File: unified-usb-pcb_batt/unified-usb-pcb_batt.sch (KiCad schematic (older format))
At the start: 38 parts, among them J1 QI, J2 USB_C_Receptacle_USB2.0, J3 USB_Out, J4 BATT, J5 THERM, SW1 SW_SPDT, U1 SRV05-4, U2 DW01A, U3 TP4056, U4 FS8205

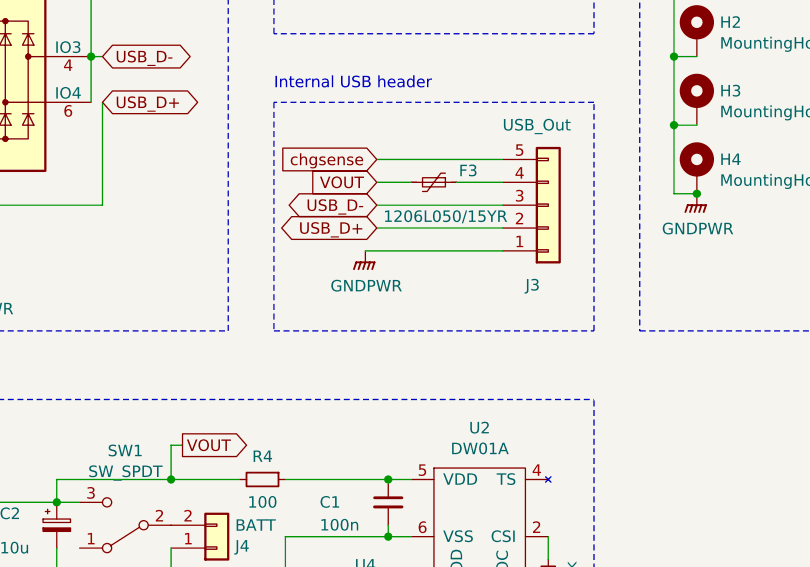
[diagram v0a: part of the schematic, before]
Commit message: added ferrite bead
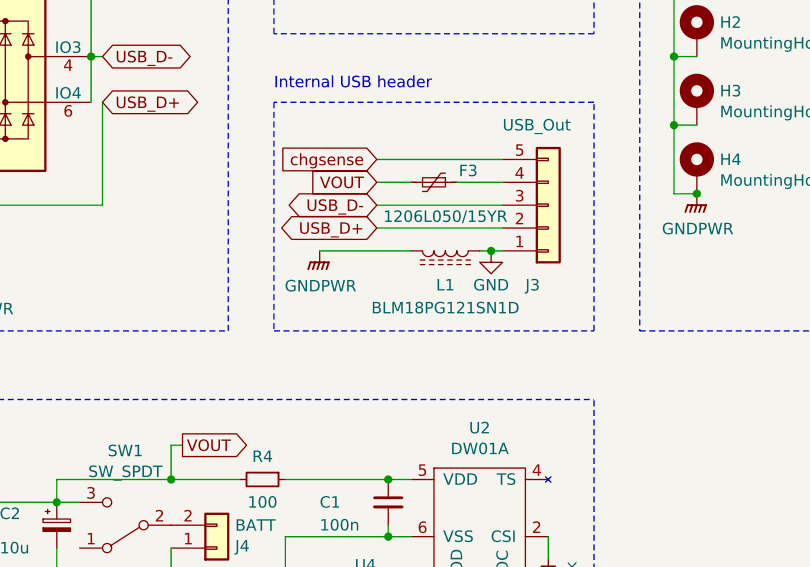
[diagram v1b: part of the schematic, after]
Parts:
- added L1: BLM18PG121SN1D, Inductor_SMD:L_0603_1608Metric, symbol Device:L_Core_Ferrite
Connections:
- net GNDPWR: now also L1.2; no longer J3.1 (Pin_1)
- new net GND: J3.1 (Pin_1), L1.1
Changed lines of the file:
@@
 L power:GNDPWR #PWR05
 U 1 1 5E879D91
-P 4550 2500
-F 0 "#PWR05" H 4550 2300 50  0001 C CNN
-F 1 "GNDPWR" H 4554 2346 50  0000 C CNN
-F 2 "" H 4550 2450 50  0001 C CNN
-F 3 "" H 4550 2450 50  0001 C CNN
-	1    4550 2500
-	1    0    0    -1
-$EndComp
-Wire Wire Line
-	5150 2500 4550 2500
+P 4350 2500
+F 0 "#PWR05" H 4350 2300 50  0001 C CNN
+F 1 "GNDPWR" H 4354 2346 50  0000 C CNN
+F 2 "" H 4350 2450 50  0001 C CNN
+F 3 "" H 4350 2450 50  0001 C CNN
+	1    4350 2500
+	1    0    0    -1
+$EndComp
 Text GLabel 4600 2100 0    50   Input ~ 0
 chgsense
@@
 Text Notes 5750 650  0    50   ~ 0
 Mounting Holes
+$Comp
+L Device:L_Core_Ferrite L1
+U 1 1 5E8FEF9F
+P 4900 2500
+F 0 "L1" V 5050 2500 50  0000 C CNN
+F 1 "BLM18PG121SN1D" V 5150 2500 50  0000 C CNN
+F 2 "Inductor_SMD:L_0603_1608Metric" H 4900 2500 50  0001 C CNN
+F 3 "~" H 4900 2500 50  0001 C CNN
+	1    4900 2500
+	0    1    1    0
+$EndComp
+Wire Wire Line
+	5150 2500 5100 2500
+Wire Wire Line
+	4750 2500 4350 2500
+$Comp
+L power:GND #PWR0102
+U 1 1 5E908A81
+P 5100 2500
+F 0 "#PWR0102" H 5100 2250 50  0001 C CNN
+F 1 "GND" H 5100 2350 50  0000 C CNN
+F 2 "" H 5100 2500 50  0001 C CNN
+F 3 "" H 5100 2500 50  0001 C CNN
+	1    5100 2500
+	1    0    0    -1
+$EndComp
+Connection ~ 5100 2500
+Wire Wire Line
+	5100 2500 5050 2500
 $EndSCHEMATC

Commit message: added jlcpcb part numbers
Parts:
- C1, C4: LCSC (none) -> C14663
- C2, C3: LCSC (none) -> C7171
- D1, D2: LCSC (none) -> C8678
- D3: LCSC (none) -> C72043
- D4: LCSC (none) -> C2286
- F1, F2, F3: LCSC (none) -> C151162
- H1, H2, H3, H4, J1, J2, J3, J4, J5, JP1, JP2, SW1: LCSC (none) -> /
- L1: LCSC (none) -> C73100
- R1, R2: LCSC (none) -> C23186
- R10: LCSC (none) -> C4177
- R11: LCSC (none) -> C31850
- R3: LCSC (none) -> C21189
- R4: LCSC (none) -> C22775
- R5, R7: LCSC (none) -> C13167
- R6: LCSC (none) -> C25804
- R8: LCSC (none) -> C22978
- R9: LCSC (none) -> C21190
- U1: LCSC (none) -> C85364
- U2: LCSC (none) -> C14213
- U3: LCSC (none) -> C16581
- U4: LCSC (none) -> C32254
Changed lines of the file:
@@
 F 2 "Connector_USB:USB_C_Receptacle_HRO_TYPE-C-31-M-12" H 1250 1700 50  0001 C CNN
 F 3 "https://www.usb.org/sites/default/files/documents/usb_type-c.zip" H 1250 1700 50  0001 C CNN
+F 4 "/" H 1100 1700 50  0001 C CNN "LCSC"
 	1    1100 1700
 	1    0    0    -1
@@
 F 2 "Package_TO_SOT_SMD:SOT-23-6" H 3550 1300 50  0001 C CNN
 F 3 "http://www.onsemi.com/pub/Collateral/SRV05-4-D.PDF" H 2850 1750 50  0001 C CNN
+F 4 "C85364" H 2850 1750 50  0001 C CNN "LCSC"
 	1    2850 1750
 	1    0    0    -1
@@
 F 2 "Resistor_SMD:R_0603_1608Metric" H 950 2600 50  0001 C CNN
 F 3 "~" H 950 2600 50  0001 C CNN
+F 4 "C21189" H 950 2600 50  0001 C CNN "LCSC"
 	1    950  2600
 	0    1    1    0
@@
 F 2 "Resistor_SMD:R_0603_1608Metric" H 1850 1300 50  0001 C CNN
 F 3 "~" H 1850 1300 50  0001 C CNN
+F 4 "C23186" H 1850 1300 50  0001 C CNN "LCSC"
 	1    1850 1300
 	0    1    1    0
@@
 F 2 "Resistor_SMD:R_0603_1608Metric" H 1850 1400 50  0001 C CNN
 F 3 "~" H 1850 1400 50  0001 C CNN
+F 4 "C23186" H 1850 1400 50  0001 C CNN "LCSC"
 	1    1850 1400
 	0    1    1    0
@@
 F 2 "Diode_SMD:D_SMA" H 3000 1100 50  0001 C CNN
 F 3 "https://datasheet.lcsc.com/szlcsc/Vishay-Intertech-SS36-E3-57T_C35722.pdf" H 3000 1100 50  0001 C CNN
+F 4 "C8678" H 3000 1100 50  0001 C CNN "LCSC"
 	1    3000 1100
 	-1   0    0    1
@@
 F 2 "Connector_JST:JST_SH_SM05B-SRSS-TB_1x05-1MP_P1.00mm_Horizontal" H 5350 2300 50  0001 C CNN
 F 3 "~" H 5350 2300 50  0001 C CNN
+F 4 "/" H 5350 2300 50  0001 C CNN "LCSC"
 	1    5350 2300
 	1    0    0    1
@@
 F 2 "Connector_JST:JST_SH_SM02B-SRSS-TB_1x02-1MP_P1.00mm_Horizontal" H 3900 3800 50  0001 C CNN
 F 3 "~" H 3900 3800 50  0001 C CNN
+F 4 "/" H 3900 3800 50  0001 C CNN "LCSC"
 	1    3900 3800
 	1    0    0    1
@@
 F 2 "Connector_JST:JST_SH_SM02B-SRSS-TB_1x02-1MP_P1.00mm_Horizontal" H 3400 4050 50  0001 C CNN
 F 3 "~" H 3400 4050 50  0001 C CNN
+F 4 "/" H 3400 4050 50  0001 C CNN "LCSC"
 	1    3400 4050
 	1    0    0    -1
@@
 F 2 "Connector_JST:JST_SH_SM02B-SRSS-TB_1x02-1MP_P1.00mm_Horizontal" H 4350 1200 50  0001 C CNN
 F 3 "~" H 4350 1200 50  0001 C CNN
+F 4 "/" H 4350 1200 50  0001 C CNN "LCSC"
 	1    4350 1200
 	-1   0    0    1
@@
 F 2 "Diode_SMD:D_SMA" H 5000 1100 50  0001 C CNN
 F 3 "https://datasheet.lcsc.com/szlcsc/Vishay-Intertech-SS36-E3-57T_C35722.pdf" H 5000 1100 50  0001 C CNN
+F 4 "C8678" H 5000 1100 50  0001 C CNN "LCSC"
 	1    5000 1100
 	-1   0    0    1
@@
 F 2 "Fuse:Fuse_1206_3216Metric" H 4750 900 50  0001 L CNN
 F 3 "https://datasheet.lcsc.com/szlcsc/1810252220_Fuzetec-Tech-FSMD050-1206-R_C220147.pdf" H 4700 1100 50  0001 C CNN
+F 4 "C151162" H 4700 1100 50  0001 C CNN "LCSC"
 	1    4700 1100
 	0    1    1    0
@@
 F 2 "Resistor_SMD:R_0603_1608Metric" H 650 3900 50  0001 C CNN
 F 3 "~" H 650 3900 50  0001 C CNN
+F 4 "C13167" H 650 3900 50  0001 C CNN "LCSC"
 	1    650  3900
 	-1   0    0    1
@@
 F 2 "Resistor_SMD:R_0603_1608Metric" H 1100 3900 50  0001 C CNN
 F 3 "~" H 1100 3900 50  0001 C CNN
+F 4 "C13167" H 1100 3900 50  0001 C CNN "LCSC"
 	1    1100 3900
 	-1   0    0    1
@@
 F 2 "LED_SMD:LED_0603_1608Metric_Castellated" V 650 3700 50  0001 C CNN
 F 3 "~" V 650 3700 50  0001 C CNN
+F 4 "C72043" H 650 3700 50  0001 C CNN "LCSC"
 	1    650  3700
 	0    -1   -1   0
@@
 F 2 "LED_SMD:LED_0603_1608Metric_Castellated" V 1100 3700 50  0001 C CNN
 F 3 "~" V 1100 3700 50  0001 C CNN
+F 4 "C2286" H 1100 3700 50  0001 C CNN "LCSC"
 	1    1100 3700
 	0    -1   -1   0
@@
 F 2 "Resistor_SMD:R_0603_1608Metric" H 2550 4250 50  0001 C CNN
 F 3 "~" H 2550 4250 50  0001 C CNN
+F 4 "C4177" H 2550 4250 50  0001 C CNN "LCSC"
 	1    2550 4250
 	-1   0    0    1
@@
 F 2 "Jumper:SolderJumper-2_P1.3mm_Open_RoundedPad1.0x1.5mm" H 3000 4250 50  0001 C CNN
 F 3 "~" H 3000 4250 50  0001 C CNN
+F 4 "/" H 3000 4250 50  0001 C CNN "LCSC"
 	1    3000 4250
 	0    1    1    0
@@
 F 2 "Jumper:SolderJumper-2_P1.3mm_Open_RoundedPad1.0x1.5mm" H 3050 900 50  0001 C CNN
 F 3 "~" H 3050 900 50  0001 C CNN
+F 4 "/" H 3050 900 50  0001 C CNN "LCSC"
 	1    3050 900
 	-1   0    0    1
@@
 F 2 "Resistor_SMD:R_0603_1608Metric" H 2800 3950 50  0001 C CNN
 F 3 "~" H 2800 3950 50  0001 C CNN
+F 4 "C22978" H 2800 3950 50  0001 C CNN "LCSC"
 	1    2800 3950
 	-1   0    0    1
@@
 F 2 "Resistor_SMD:R_0603_1608Metric" H 2800 4250 50  0001 C CNN
 F 3 "~" H 2800 4250 50  0001 C CNN
+F 4 "C31850" H 2800 4250 50  0001 C CNN "LCSC"
 	1    2800 4250
 	-1   0    0    1
@@
 F 2 "Capacitor_Tantalum_SMD:CP_EIA-3216-18_Kemet-A" H 1400 3800 50  0001 C CNN
 F 3 "~" H 1400 3800 50  0001 C CNN
+F 4 "C7171" H 1400 3800 50  0001 C CNN "LCSC"
 	1    1400 3800
 	1    0    0    -1
@@
 F 2 "Capacitor_SMD:C_0603_1608Metric" H 4650 3600 50  0001 C CNN
 F 3 "~" H 4650 3600 50  0001 C CNN
+F 4 "C14663" H 4650 3600 50  0001 C CNN "LCSC"
 	1    4650 3600
 	1    0    0    -1
@@
 F 2 "Resistor_SMD:R_0603_1608Metric" H 5350 3950 50  0001 C CNN
 F 3 "~" H 5350 3950 50  0001 C CNN
+F 4 "C21190" H 5350 3950 50  0001 C CNN "LCSC"
 	1    5350 3950
 	-1   0    0    1
@@
 F 2 "Resistor_SMD:R_0603_1608Metric" H 4100 3500 50  0001 C CNN
 F 3 "~" H 4100 3500 50  0001 C CNN
+F 4 "C22775" H 4100 3500 50  0001 C CNN "LCSC"
 	1    4100 3500
 	0    1    1    0
@@
 F 2 "Capacitor_Tantalum_SMD:CP_EIA-3216-18_Kemet-A" H 3200 3700 50  0001 C CNN
 F 3 "~" H 3200 3700 50  0001 C CNN
+F 4 "C7171" H 3200 3700 50  0001 C CNN "LCSC"
 	1    3200 3700
 	1    0    0    -1
@@
 F 2 "Capacitor_SMD:C_0603_1608Metric" H 1650 3800 50  0001 C CNN
 F 3 "~" H 1650 3800 50  0001 C CNN
+F 4 "C14663" H 1650 3800 50  0001 C CNN "LCSC"
 	1    1650 3800
 	1    0    0    -1
@@
 F 2 "Fuse:Fuse_1206_3216Metric" H 1900 900 50  0001 L CNN
 F 3 "https://datasheet.lcsc.com/szlcsc/1810252220_Fuzetec-Tech-FSMD050-1206-R_C220147.pdf" H 1850 1100 50  0001 C CNN
+F 4 "C151162" H 1850 1100 50  0001 C CNN "LCSC"
 	1    1850 1100
 	0    1    1    0
@@
 F 2 "Fuse:Fuse_1206_3216Metric" H 4900 2000 50  0001 L CNN
 F 3 "https://datasheet.lcsc.com/szlcsc/1810252220_Fuzetec-Tech-FSMD050-1206-R_C220147.pdf" H 4850 2200 50  0001 C CNN
+F 4 "C151162" H 4850 2200 50  0001 C CNN "LCSC"
 	1    4850 2200
 	0    1    1    0
@@
 F 2 "Resistor_SMD:R_0603_1608Metric" H 850 3900 50  0001 C CNN
 F 3 "~" H 850 3900 50  0001 C CNN
+F 4 "C25804" H 850 3900 50  0001 C CNN "LCSC"
 	1    850  3900
 	-1   0    0    1
@@
 F 2 "Package_SO:SOIC-8-1EP_3.9x4.9mm_P1.27mm_EP2.29x3mm" H 2150 4350 50  0001 C CNN
 F 3 "https://datasheet.lcsc.com/szlcsc/1906261508_Nanjing-Extension-Microelectronics-TP4056-42-ESOP8_C16581.pdf" H 2150 4350 50  0001 C CNN
+F 4 "C16581" H 2200 3850 50  0001 C CNN "LCSC"
 	1    2200 3850
 	1    0    0    -1
@@
 F 2 "Package_TO_SOT_SMD:SOT-23-6" H 4850 4050 50  0001 C CNN
 F 3 "https://datasheet.lcsc.com/szlcsc/Fortune-Semicon-DW01A-G_C61503.pdf" H 4850 4050 50  0001 C CNN
+F 4 "C14213" H 5050 3700 50  0001 C CNN "LCSC"
 	1    5050 3700
 	1    0    0    -1
@@
 F 2 "Package_TO_SOT_SMD:SOT-23-6" H 4500 4450 50  0001 C CNN
 F 3 "https://datasheet.lcsc.com/szlcsc/Fortune-Semicon-FS8205_C32254.pdf" H 4500 4450 50  0001 C CNN
+F 4 "C32254" H 4550 4200 50  0001 C CNN "LCSC"
 	1    4550 4200
 	1    0    0    -1
@@
 F 2 "kicad-keyboard-parts:ESP3020" H 3500 3700 50  0001 C CNN
 F 3 "https://www.ece.com.tw/images/cgcustom/file020190722095856.pdf" H 3500 3700 50  0001 C CNN
+F 4 "/" H 3500 3700 50  0001 C CNN "LCSC"
 	1    3500 3700
 	-1   0    0    1
@@
 F 2 "MountingHole:MountingHole_2.7mm_M2.5_DIN965_Pad" H 6000 1250 50  0001 C CNN
 F 3 "~" H 6000 1250 50  0001 C CNN
+F 4 "/" H 6000 1250 50  0001 C CNN "LCSC"
 	1    6000 1250
 	1    0    0    -1
@@
 F 2 "MountingHole:MountingHole_2.7mm_M2.5_DIN965_Pad" H 6000 1550 50  0001 C CNN
 F 3 "~" H 6000 1550 50  0001 C CNN
+F 4 "/" H 6000 1550 50  0001 C CNN "LCSC"
 	1    6000 1550
 	1    0    0    -1
@@
 F 2 "MountingHole:MountingHole_2.7mm_M2.5_DIN965_Pad" H 6000 1850 50  0001 C CNN
 F 3 "~" H 6000 1850 50  0001 C CNN
+F 4 "/" H 6000 1850 50  0001 C CNN "LCSC"
 	1    6000 1850
 	1    0    0    -1
@@
 F 2 "MountingHole:MountingHole_2.7mm_M2.5_DIN965_Pad" H 6000 2150 50  0001 C CNN
 F 3 "~" H 6000 2150 50  0001 C CNN
+F 4 "/" H 6000 2150 50  0001 C CNN "LCSC"
 	1    6000 2150
 	1    0    0    -1
@@
 F 2 "Inductor_SMD:L_0603_1608Metric" H 4900 2500 50  0001 C CNN
 F 3 "~" H 4900 2500 50  0001 C CNN
+F 4 "C73100" H 4900 2500 50  0001 C CNN "LCSC"
 	1    4900 2500
 	0    1    1    0

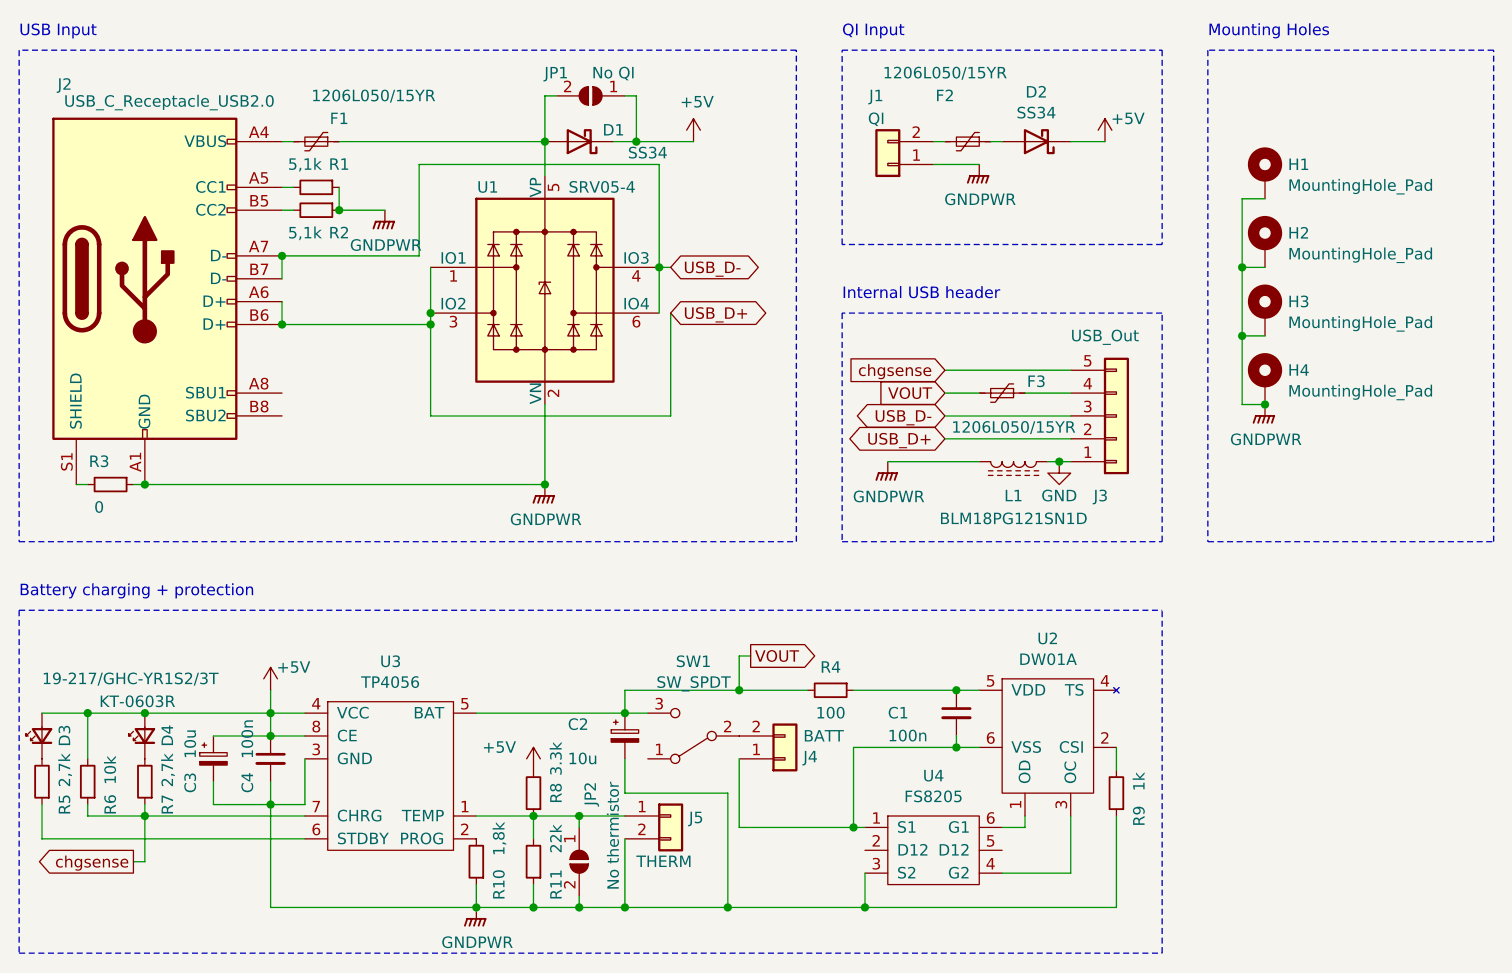
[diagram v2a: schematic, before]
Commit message: changed jumper pad, fixed silk
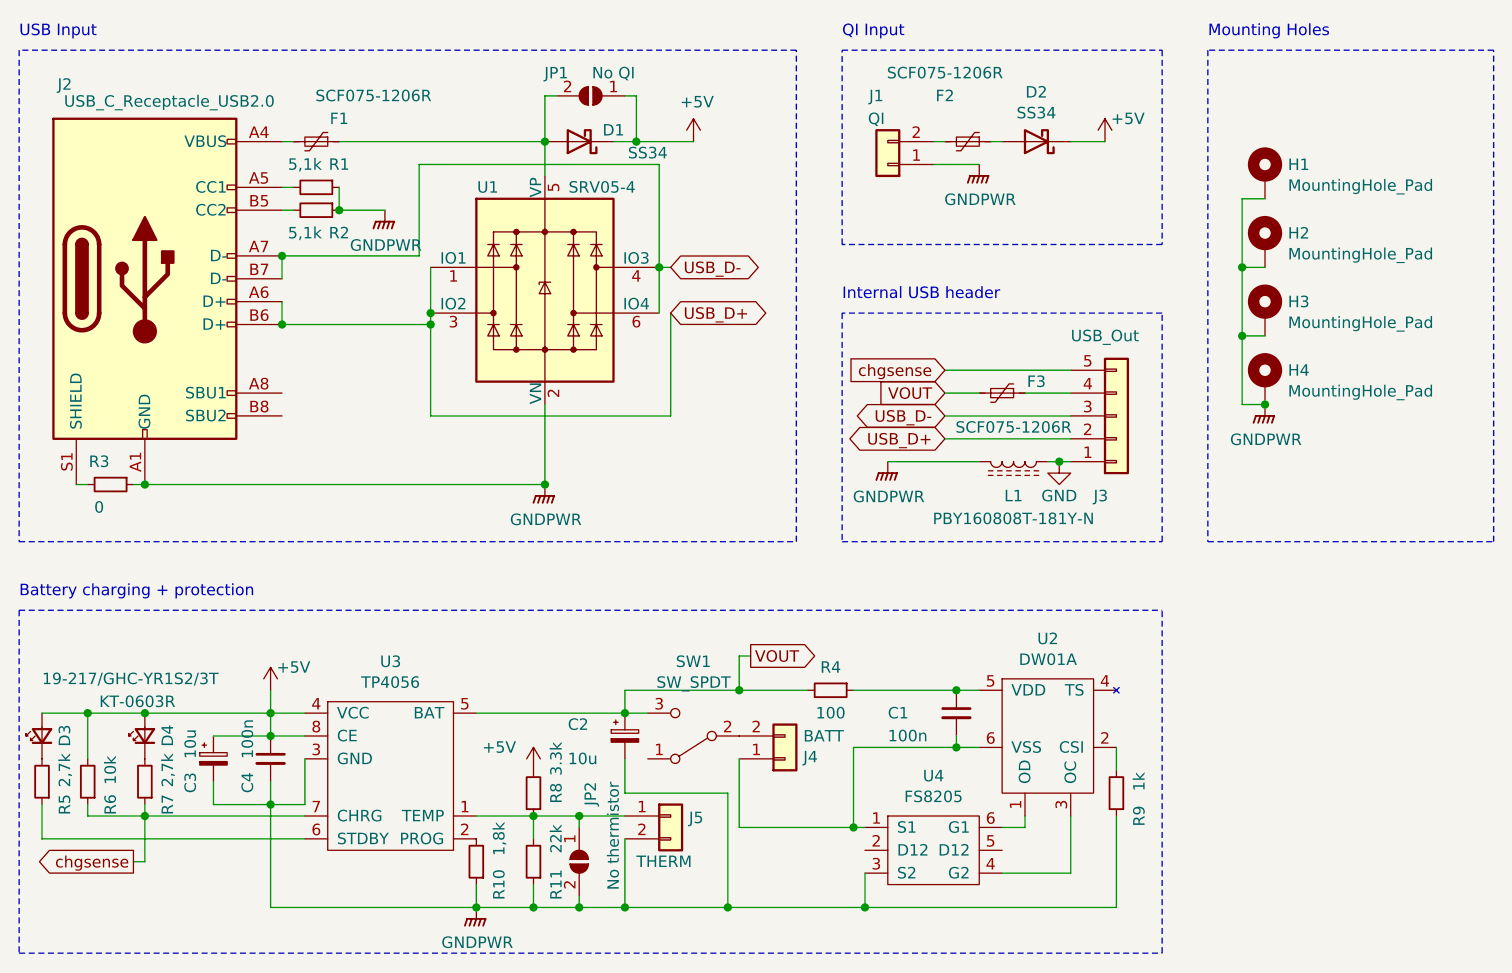
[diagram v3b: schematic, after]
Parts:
- F1, F2, F3: value 1206L050/15YR -> SCF075-1206R; LCSC C151162 -> C183290
- JP1, JP2: footprint Jumper:SolderJumper-2_P1.3mm_Open_RoundedPad1.0x1.5mm -> Jumper:SolderJumper-2_P1.3mm_Open_Pad1.0x1.5mm
- L1: value BLM18PG121SN1D -> PBY160808T-181Y-N; LCSC C73100 -> C114288
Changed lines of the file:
@@
 P 4700 1100
 F 0 "F2" V 4500 1000 50  0000 C CNN
-F 1 "1206L050/15YR" V 4400 1000 50  0000 C CNN
+F 1 "SCF075-1206R" V 4400 1000 50  0000 C CNN
 F 2 "Fuse:Fuse_1206_3216Metric" H 4750 900 50  0001 L CNN
 F 3 "https://datasheet.lcsc.com/szlcsc/1810252220_Fuzetec-Tech-FSMD050-1206-R_C220147.pdf" H 4700 1100 50  0001 C CNN
-F 4 "C151162" H 4700 1100 50  0001 C CNN "LCSC"
+F 4 "C183290" H 4700 1100 50  0001 C CNN "LCSC"
 	1    4700 1100
 	0    1    1    0
@@
 F 0 "JP2" H 2650 4300 50  0000 L CNN
 F 1 "No thermistor" H 2650 4400 50  0000 L CNN
-F 2 "Jumper:SolderJumper-2_P1.3mm_Open_RoundedPad1.0x1.5mm" H 3000 4250 50  0001 C CNN
+F 2 "Jumper:SolderJumper-2_P1.3mm_Open_Pad1.0x1.5mm" H 3000 4250 50  0001 C CNN
 F 3 "~" H 3000 4250 50  0001 C CNN
 F 4 "/" H 3000 4250 50  0001 C CNN "LCSC"
@@
 F 0 "JP1" H 3200 800 50  0000 C CNN
 F 1 "No QI" H 2950 800 50  0000 C CNN
-F 2 "Jumper:SolderJumper-2_P1.3mm_Open_RoundedPad1.0x1.5mm" H 3050 900 50  0001 C CNN
+F 2 "Jumper:SolderJumper-2_P1.3mm_Open_Pad1.0x1.5mm" H 3050 900 50  0001 C CNN
 F 3 "~" H 3050 900 50  0001 C CNN
 F 4 "/" H 3050 900 50  0001 C CNN "LCSC"
@@
 P 1850 1100
 F 0 "F1" V 1750 1200 50  0000 C CNN
-F 1 "1206L050/15YR" V 1650 1350 50  0000 C CNN
+F 1 "SCF075-1206R" V 1650 1350 50  0000 C CNN
 F 2 "Fuse:Fuse_1206_3216Metric" H 1900 900 50  0001 L CNN
 F 3 "https://datasheet.lcsc.com/szlcsc/1810252220_Fuzetec-Tech-FSMD050-1206-R_C220147.pdf" H 1850 1100 50  0001 C CNN
-F 4 "C151162" H 1850 1100 50  0001 C CNN "LCSC"
+F 4 "C183290" H 1850 1100 50  0001 C CNN "LCSC"
 	1    1850 1100
 	0    1    1    0
@@
 P 4850 2200
 F 0 "F3" V 4800 2350 50  0000 C CNN
-F 1 "1206L050/15YR" V 5000 2250 50  0000 C CNN
+F 1 "SCF075-1206R" V 5000 2250 50  0000 C CNN
 F 2 "Fuse:Fuse_1206_3216Metric" H 4900 2000 50  0001 L CNN
 F 3 "https://datasheet.lcsc.com/szlcsc/1810252220_Fuzetec-Tech-FSMD050-1206-R_C220147.pdf" H 4850 2200 50  0001 C CNN
-F 4 "C151162" H 4850 2200 50  0001 C CNN "LCSC"
+F 4 "C183290" H 4850 2200 50  0001 C CNN "LCSC"
 	1    4850 2200
 	0    1    1    0
@@
 P 4900 2500
 F 0 "L1" V 5050 2500 50  0000 C CNN
-F 1 "BLM18PG121SN1D" V 5150 2500 50  0000 C CNN
+F 1 "PBY160808T-181Y-N" V 5150 2500 50  0000 C CNN
 F 2 "Inductor_SMD:L_0603_1608Metric" H 4900 2500 50  0001 C CNN
 F 3 "~" H 4900 2500 50  0001 C CNN
-F 4 "C73100" H 4900 2500 50  0001 C CNN "LCSC"
+F 4 "C114288" H 4900 2500 50  0001 C CNN "LCSC"
 	1    4900 2500
 	0    1    1    0
